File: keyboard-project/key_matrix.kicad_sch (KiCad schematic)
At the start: 0 parts

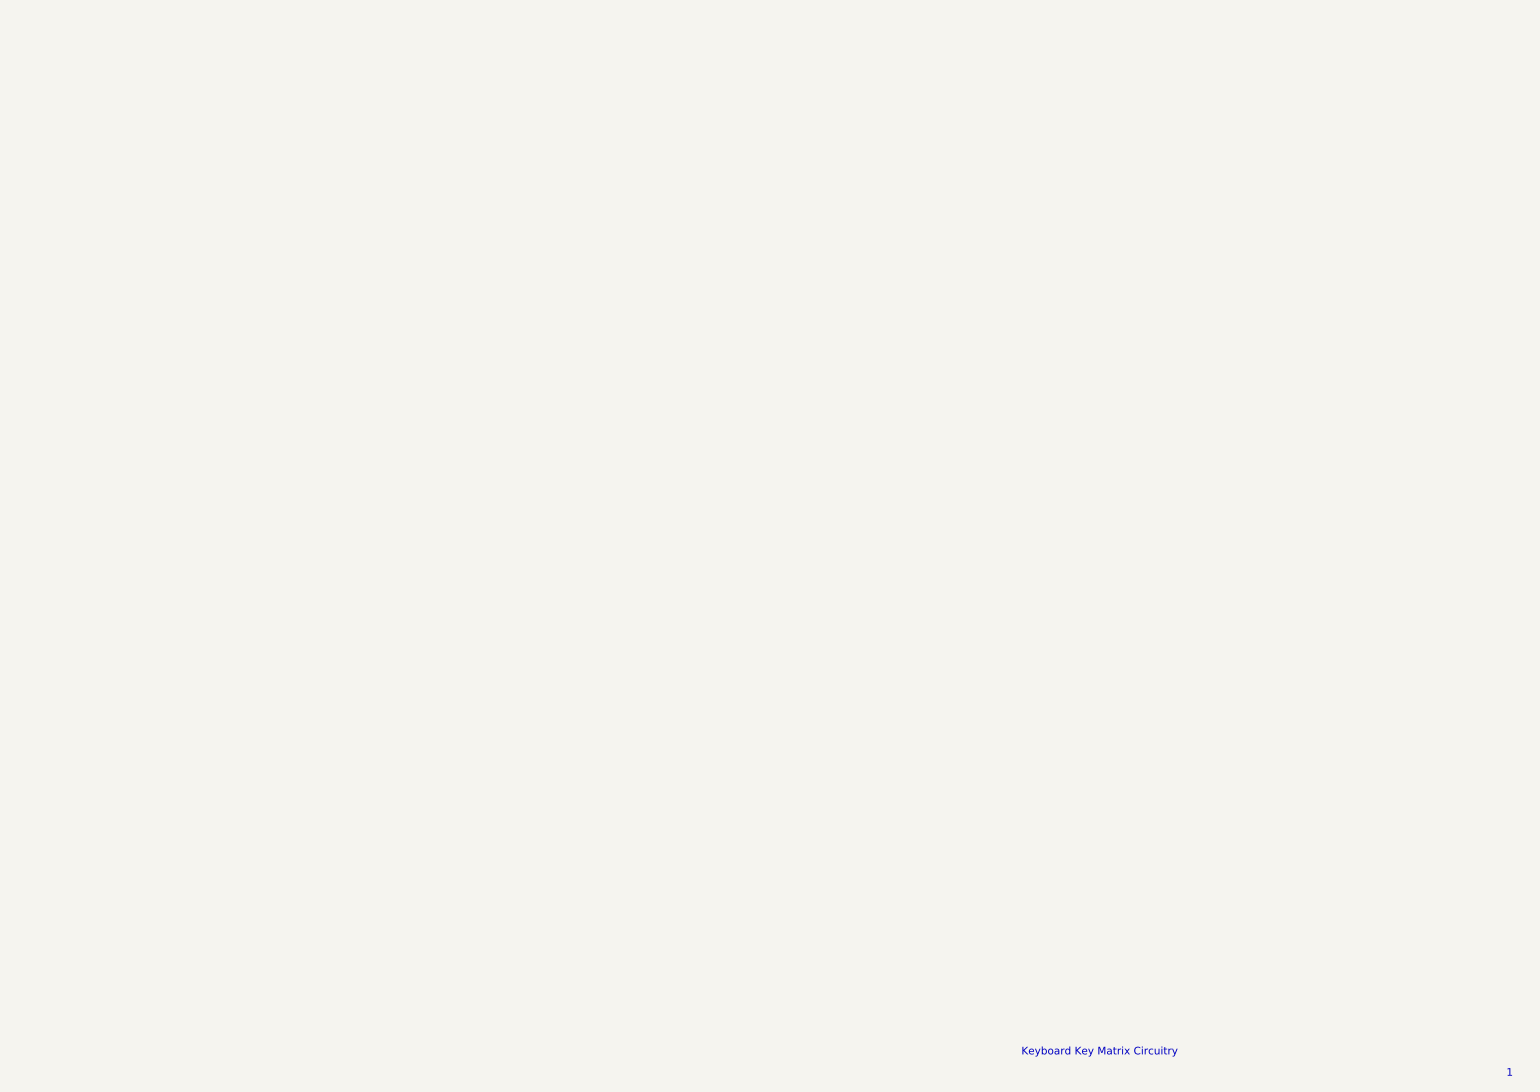
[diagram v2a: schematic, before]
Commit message: encoders, trackball, and display circuits
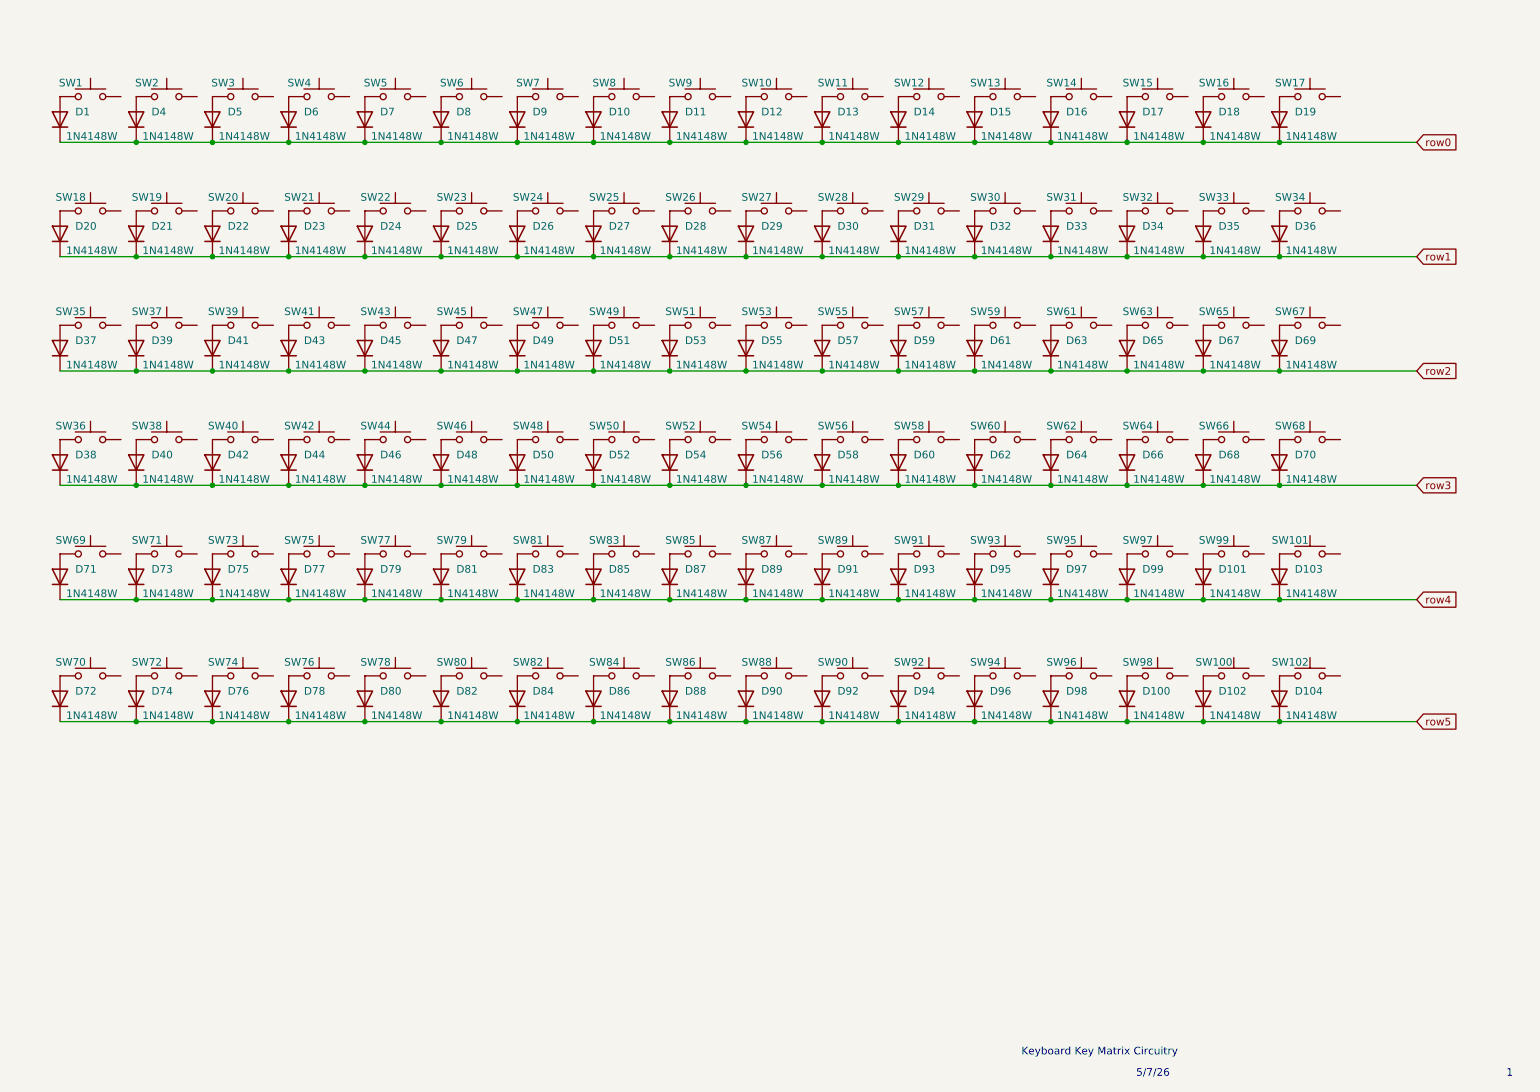
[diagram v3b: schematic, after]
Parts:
- added D1, D10, D100, D101, D102, D103, D104, D11, D12, D13, D14, D15, D16, D17, D18, D19, D20, D21, D22, D23, D24, D25, D26, D27, D28, D29, D30, D31, D32, D33, D34, D35, D36, D37, D38, D39, D4, D40, D41, D42, D43, D44, D45, D46, D47, D48, D49, D5, D50, D51, D52, D53, D54, D55, D56, D57, D58, D59, D6, D60, D61, D62, D63, D64, D65, D66, D67, D68, D69, D7, D70, D71, D72, D73, D74, D75, D76, D77, D78, D79, D8, D80, D81, D82, D83, D84, D85, D86, D87, D88, D89, D9, D90, D91, D92, D93, D94, D95, D96, D97, D98, D99: 1N4148W, Diode_SMD:D_SOD-123, symbol Diode:1N4148W
- added SW1, SW10, SW100, SW101, SW102, SW11, SW12, SW13, SW14, SW15, SW16, SW17, SW18, SW19, SW2, SW20, SW21, SW22, SW23, SW24, SW25, SW26, SW27, SW28, SW29, SW3, SW30, SW31, SW32, SW33, SW34, SW35, SW36, SW37, SW38, SW39, SW4, SW40, SW41, SW42, SW43, SW44, SW45, SW46, SW47, SW48, SW49, SW5, SW50, SW51, SW52, SW53, SW54, SW55, SW56, SW57, SW58, SW59, SW6, SW60, SW61, SW62, SW63, SW64, SW65, SW66, SW67, SW68, SW69, SW7, SW70, SW71, SW72, SW73, SW74, SW75, SW76, SW77, SW78, SW79, SW8, SW80, SW81, SW82, SW83, SW84, SW85, SW86, SW87, SW88, SW89, SW9, SW90, SW91, SW92, SW93, SW94, SW95, SW96, SW97, SW98, SW99: SW_Push, symbol Switch:SW_Push
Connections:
- new net: D39.2 (A), SW37.1
- new net: D42.2 (A), SW40.1
- new net: D32.2 (A), SW30.1
- new net: D50.2 (A), SW48.1
- new net: D51.2 (A), SW49.1
- new net: D41.2 (A), SW39.1
- new net: D26.2 (A), SW24.1
- new net: D27.2 (A), SW25.1
- new net: D1.2 (A), SW1.1
- new net: D7.2 (A), SW5.1
- new net: D28.2 (A), SW26.1
- new net: D18.2 (A), SW16.1
- new net: D38.2 (A), SW36.1
- new net: D98.2 (A), SW96.1
- new net: D104.2 (A), SW102.1
- new net: D24.2 (A), SW22.1
- new net: D36.2 (A), SW34.1
- new net: D17.2 (A), SW15.1
- new net: D19.2 (A), SW17.1
- new net: D53.2 (A), SW51.1
- new net: D40.2 (A), SW38.1
- new net: D82.2 (A), SW80.1
- new net: D55.2 (A), SW53.1
- new net: D64.2 (A), SW62.1
- new net: D57.2 (A), SW55.1
- new net: D61.2 (A), SW59.1
- new net: D20.2 (A), SW18.1
- new net: D102.2 (A), SW100.1
- new net: D31.2 (A), SW29.1
- new net: D94.2 (A), SW92.1
- new net: D21.2 (A), SW19.1
- new net: D78.2 (A), SW76.1
- new net: D48.2 (A), SW46.1
- new net: D62.2 (A), SW60.1
- new net: D97.2 (A), SW95.1
- new net: D88.2 (A), SW86.1
- new net: D45.2 (A), SW43.1
- new net: D5.2 (A), SW3.1
- new net: D11.2 (A), SW9.1
- new net: D95.2 (A), SW93.1
- new net: D29.2 (A), SW27.1
- new net: D63.2 (A), SW61.1
- new net: D75.2 (A), SW73.1
- new net: D84.2 (A), SW82.1
- new net: D86.2 (A), SW84.1
- new net: D70.2 (A), SW68.1
- new net: D92.2 (A), SW90.1
- new net: D83.2 (A), SW81.1
- new net: D80.2 (A), SW78.1
- new net: D44.2 (A), SW42.1
- new net: D16.2 (A), SW14.1
- new net: D14.2 (A), SW12.1
- new net: D81.2 (A), SW79.1
- new net: D66.2 (A), SW64.1
- new net: D96.2 (A), SW94.1
- new net: D67.2 (A), SW65.1
- new net: D68.2 (A), SW66.1
- new net: D9.2 (A), SW7.1
- new net: D49.2 (A), SW47.1
- new net: D6.2 (A), SW4.1
- new net: D12.2 (A), SW10.1
- new net: D54.2 (A), SW52.1
- new net: D59.2 (A), SW57.1
- new net: D65.2 (A), SW63.1
- new net: D47.2 (A), SW45.1
- new net: D58.2 (A), SW56.1
- new net: D101.2 (A), SW99.1
- new net: D8.2 (A), SW6.1
- new net: D103.2 (A), SW101.1
- new net: D74.2 (A), SW72.1
- new net: D37.2 (A), SW35.1
- new net: D91.2 (A), SW89.1
- new net: D72.2 (A), SW70.1
- new net: D71.2 (A), SW69.1
- new net: D77.2 (A), SW75.1
- new net: D73.2 (A), SW71.1
- new net: D87.2 (A), SW85.1
- new net: D100.2 (A), SW98.1
- new net: D25.2 (A), SW23.1
- new net: D85.2 (A), SW83.1
- new net: D4.2 (A), SW2.1
- new net: D15.2 (A), SW13.1
- new net: D43.2 (A), SW41.1
- new net: D34.2 (A), SW32.1
- new net: D69.2 (A), SW67.1
- new net: D60.2 (A), SW58.1
- new net: D79.2 (A), SW77.1
- new net: D89.2 (A), SW87.1
- new net: D10.2 (A), SW8.1
- new net: D30.2 (A), SW28.1
- new net: D56.2 (A), SW54.1
- new net: D46.2 (A), SW44.1
- new net: D13.2 (A), SW11.1
- new net: D99.2 (A), SW97.1
- new net: D90.2 (A), SW88.1
- new net: D22.2 (A), SW20.1
- new net: D35.2 (A), SW33.1
- new net: D52.2 (A), SW50.1
- new net: D93.2 (A), SW91.1
- new net: D23.2 (A), SW21.1
- new net: D76.2 (A), SW74.1
- new net: D33.2 (A), SW31.1
- new net row0: D1.1 (K), D10.1 (K), D11.1 (K), D12.1 (K), D13.1 (K), D14.1 (K), D15.1 (K), D16.1 (K), D17.1 (K), D18.1 (K), D19.1 (K), D4.1 (K), D5.1 (K), D6.1 (K), D7.1 (K), D8.1 (K), D9.1 (K)
- new net row1: D20.1 (K), D21.1 (K), D22.1 (K), D23.1 (K), D24.1 (K), D25.1 (K), D26.1 (K), D27.1 (K), D28.1 (K), D29.1 (K), D30.1 (K), D31.1 (K), D32.1 (K), D33.1 (K), D34.1 (K), D35.1 (K), D36.1 (K)
- new net row2: D37.1 (K), D39.1 (K), D41.1 (K), D43.1 (K), D45.1 (K), D47.1 (K), D49.1 (K), D51.1 (K), D53.1 (K), D55.1 (K), D57.1 (K), D59.1 (K), D61.1 (K), D63.1 (K), D65.1 (K), D67.1 (K), D69.1 (K)
- new net row3: D38.1 (K), D40.1 (K), D42.1 (K), D44.1 (K), D46.1 (K), D48.1 (K), D50.1 (K), D52.1 (K), D54.1 (K), D56.1 (K), D58.1 (K), D60.1 (K), D62.1 (K), D64.1 (K), D66.1 (K), D68.1 (K), D70.1 (K)
- new net row4: D101.1 (K), D103.1 (K), D71.1 (K), D73.1 (K), D75.1 (K), D77.1 (K), D79.1 (K), D81.1 (K), D83.1 (K), D85.1 (K), D87.1 (K), D89.1 (K), D91.1 (K), D93.1 (K), D95.1 (K), D97.1 (K), D99.1 (K)
- new net row5: D100.1 (K), D102.1 (K), D104.1 (K), D72.1 (K), D74.1 (K), D76.1 (K), D78.1 (K), D80.1 (K), D82.1 (K), D84.1 (K), D86.1 (K), D88.1 (K), D90.1 (K), D92.1 (K), D94.1 (K), D96.1 (K), D98.1 (K)
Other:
- note added: "5/7/26"

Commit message: all footprints in now
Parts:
- removed D101, D102, D103, D104, D16, D64, D66, D68, D70, D78, D80, D84, D86: 1N4148W, Diode_SMD:D_SOD-123, symbol Diode:1N4148W
- removed SW100, SW101, SW102, SW90, SW91, SW92, SW93, SW94, SW95, SW96, SW97, SW98, SW99: SW_Push, symbol Switch:SW_Push
- SW1, SW10, SW11, SW12, SW13, SW14, SW15, SW16, SW17, SW18, SW19, SW2, SW20, SW21, SW22, SW23, SW24, SW25, SW26, SW27, SW28, SW29, SW3, SW31, SW32, SW33, SW34, SW35, SW36, SW37, SW38, SW39, SW4, SW40, SW41, SW42, SW43, SW44, SW45, SW46, SW47, SW48, SW5, SW51, SW52, SW53, SW54, SW55, SW56, SW57, SW58, SW59, SW6, SW60, SW61, SW65, SW66, SW67, SW68, SW69, SW7, SW70, SW71, SW72, SW73, SW74, SW76, SW77, SW78, SW79, SW8, SW88, SW89, SW9: footprint (none) -> Button_Switch_Keyboard:SW_Cherry_MX_1.00u_PCB
- SW30: footprint (none) -> Button_Switch_Keyboard:SW_Cherry_MX_2.00u_PCB
- SW49, SW50: footprint (none) -> Button_Switch_Keyboard:SW_Cherry_MX_1.50u_PCB
- SW62, SW64: footprint (none) -> Button_Switch_Keyboard:SW_Cherry_MX_2.25u_PCB
- SW63: footprint (none) -> Button_Switch_Keyboard:SW_Cherry_MX_1.75u_PCB
- SW75: footprint (none) -> Button_Switch_Keyboard:SW_Cherry_MX_2.75u_PCB
- SW80, SW81, SW82, SW83, SW84, SW85, SW86: footprint (none) -> Button_Switch_Keyboard:SW_Cherry_MX_1.25u_PCB
- SW87: footprint (none) -> Button_Switch_Keyboard:SW_Cherry_MX_6.25u_PCB
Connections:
- net at D39.2 (A): now also SW34.1; no longer SW37.1
- net Matrix Col 4: now reaches SW37.2
- net Matrix Col 4: now also SW21.2, SW5.2, SW54.2, SW68.2
- net at D42.2 (A): now also SW52.1; no longer SW40.1
- net at D32.2 (A): now also SW29.1; no longer SW30.1
- net Matrix Col 13: now reaches SW30.2
- net Matrix Col 13: now also SW49.2, SW76.2
- net at D50.2 (A): now also SW56.1; no longer SW48.1
- net at D51.2 (A): now also SW40.1; no longer SW49.1
- net at D41.2 (A): now also SW35.1; no longer SW39.1
- net Matrix Col 6: now reaches SW39.2
- net Matrix Col 6: now also SW23.2, SW56.2, SW7.2, SW70.2
- net at D26.2 (A): now also SW23.1; no longer SW24.1
- net at SW25.1: now also D28.2 (A); no longer D27.2 (A)
- net Matrix Col 8: now reaches SW25.2
- net Matrix Col 8: now also SW41.2, SW58.2, SW72.2, SW83.2, SW9.2
- net at SW26.1: now also D29.2 (A); no longer D28.2 (A)
- net at SW16.1: now also D19.2 (A); no longer D18.2 (A)
- net Matrix Col 16: now reaches SW16.2
- net Matrix Col 16: now also SW33.2, SW48.2, SW79.2
- net at D38.2 (A): now also SW63.1; no longer SW36.1
- net at D98.2 (A): now also SW77.1
- net at D24.2 (A): now also SW21.1; no longer SW22.1
- net at D36.2 (A): now also SW33.1; no longer SW34.1
- net Matrix Col 1: now reaches SW34.2
- net Matrix Col 1: now also SW18.2, SW2.2, SW51.2, SW65.2, SW81.2
- net at D17.2 (A): now also SW14.1; no longer SW15.1
- net at SW17.1: now also D20.2 (A); no longer D19.2 (A)
- net at D53.2 (A): now also SW41.1; no longer SW51.1
- net at SW38.1: now also D47.2 (A); no longer D40.2 (A)
- net Matrix Col 5: now reaches SW38.2
- net Matrix Col 5: now also SW22.2, SW55.2, SW6.2, SW69.2, SW87.2
- net at SW80.1: now also D72.2 (A); no longer D82.2 (A)
- net at D55.2 (A): now also SW42.1; no longer SW53.1
- net Matrix Col 3: now reaches SW53.2
- net Matrix Col 3: now also SW20.2, SW36.2, SW4.2, SW67.2
- net at SW62.1: now also D62.2 (A)
- net Matrix Col 12: now reaches SW62.2
- net Matrix Col 12: now also SW13.2, SW29.2, SW45.2
- net at SW55.1: now also D48.2 (A); no longer D57.2 (A)
- net at D61.2 (A): now also SW45.1; no longer SW59.1
- net Matrix Col 9: now reaches SW59.2
- net Matrix Col 9: now also SW10.2, SW26.2, SW42.2, SW73.2, SW84.2
- net at SW18.1: now also D21.2 (A); no longer D20.2 (A)
- net at D31.2 (A): now also SW28.1; no longer SW29.1
- net at D94.2 (A): now also SW86.1
- net at SW19.1: now also D22.2 (A); no longer D21.2 (A)
- net Matrix Col 2: now reaches SW19.2
- net Matrix Col 2: now also SW3.2, SW35.2, SW52.2, SW66.2, SW82.2
- net at SW76.1: now also D95.2 (A)
- net at SW46.1: now also D65.2 (A); no longer D48.2 (A)
- net Matrix Col 14: now reaches SW46.2
- net Matrix Col 14: now also SW14.2, SW31.2, SW77.2
- net at SW60.1: now also D58.2 (A); no longer D62.2 (A)
- net Matrix Col 10: now reaches SW60.2
- net Matrix Col 10: now also SW11.2, SW27.2, SW43.2, SW74.2, SW85.2
- net at D97.2 (A): now also SW89.1
- net at D88.2 (A): now also SW83.1; no longer SW86.1
- net Matrix Col 11: now reaches SW86.2
- net Matrix Col 11: now also SW12.2, SW28.2, SW44.2, SW61.2, SW75.2
- net at D45.2 (A): now also SW37.1; no longer SW43.1
- net at SW27.1: now also D30.2 (A); no longer D29.2 (A)
- net at SW61.1: now also D60.2 (A); no longer D63.2 (A)
- net at SW73.1: now also D89.2 (A); no longer D75.2 (A)
- net at SW82.1: now also D76.2 (A)
- net Matrix Col 7: now reaches SW24.2
- net Matrix Col 7: now also SW40.2, SW57.2, SW71.2, SW8.2
- net at SW84.1: now also D90.2 (A)
- net at SW68.1: now also D79.2 (A)
- net at D92.2 (A): now also SW85.1
- net at SW81.1: now also D74.2 (A); no longer D83.2 (A)
- net at SW78.1: now also D99.2 (A)
- net at D44.2 (A): now also SW53.1; no longer SW42.1
- net at SW79.1: now also D100.2 (A); no longer D81.2 (A)
- net at SW64.1: now also D71.2 (A)
- net at D96.2 (A): now also SW88.1
- net at D67.2 (A): now also SW47.1; no longer SW65.1
- net at SW66.1: now also D75.2 (A)
- net at D49.2 (A): now also SW39.1; no longer SW47.1
- net Matrix Col 15: now reaches SW47.2
- net Matrix Col 15: now also SW15.2, SW32.2, SW78.2
- net at D54.2 (A): now also SW58.1; no longer SW52.1
- net at D59.2 (A): now also SW44.1; no longer SW57.1
- net at SW72.1: now also D87.2 (A); no longer D74.2 (A)
- net at D37.2 (A): now also SW50.1; no longer SW35.1
- net at D91.2 (A): now also SW74.1; no longer SW89.1
- net at SW70.1: now also D83.2 (A); no longer D72.2 (A)
- net at SW69.1: now also D81.2 (A); no longer D71.2 (A)
- net at D77.2 (A): now also SW67.1; no longer SW75.1
- net at D73.2 (A): now also SW65.1; no longer SW71.1
- net at D25.2 (A): now also SW22.1; no longer SW23.1
- net at D85.2 (A): now also SW71.1; no longer SW83.1
- net at D43.2 (A): now also SW36.1; no longer SW41.1
- net at D34.2 (A): now also SW31.1; no longer SW32.1
- net Matrix Col 0: now reaches SW17.2
- net Matrix Col 0: now also SW1.2, SW50.2, SW63.2, SW64.2, SW80.2
- net at D69.2 (A): now also SW48.1; no longer SW67.1
- net at SW87.1: now also D82.2 (A); no longer D89.2 (A)
- net at D56.2 (A): now also SW59.1; no longer SW54.1
- net at D46.2 (A): now also SW54.1; no longer SW44.1
- net at SW20.1: now also D23.2 (A); no longer D22.2 (A)
- net at D35.2 (A): now also SW32.1; no longer SW33.1
- net at D52.2 (A): now also SW57.1; no longer SW50.1
- net at D93.2 (A): now also SW75.1
- net at D33.2 (A): now also SW30.1; no longer SW31.1
- net row0 renamed Matrix Row 0
- net row1 renamed Matrix Row 1
- net row2 renamed Matrix Row 2
- net row3 renamed Matrix Row 3
- net row4 renamed Matrix Row 4
- net Matrix Row 4: no longer D97.1 (K), D99.1 (K)
- net row5 renamed Matrix Row 5
- net Matrix Row 5: now also D97.1 (K), D99.1 (K)
- new net: D27.2 (A), SW24.1
- new net: D18.2 (A), SW15.1
- new net: D63.2 (A), SW49.1
- new net: D57.2 (A), SW43.1
- new net: D40.2 (A), SW51.1
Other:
- note added: "'""
- note added: ",<"
- note added: "-_"
- note added: ".>"
- note added: "/?"
- note added: "0"
- note added: "2"
- note added: "3"
- note added: "4"
- note added: "5"
- note added: "6"
- note added: "7"
- note added: "8"
- note added: "9"
- note added: ";:"
- note added: "=+"
- note added: "A"
- note added: "B"
- note added: "Backspace"
- note added: "C"
- note added: "Caps Lck"
- note added: "Context"
- note added: "D"
- note added: "Del"
- note added: "Down Arrow"
- note added: "E"
- note added: "ESC"
- note added: "End"
- note added: "Enter"
- note added: "F"
- note added: "F1"
- note added: "F10"
- note added: "F11"
- note added: "F12"
- note added: "F2"
- note added: "F3"
- note added: "F4"
- note added: "F5"
- note added: "F6"
- note added: "F7"
- note added: "F8"
- note added: "F9"
- note added: "G"
- note added: "H"
- note added: "Home"
- note added: "I"
- note added: "Ins"
- note added: "J"
- note added: "K"
- note added: "L"
- note added: "L Alt"
- note added: "L Ctrl"
- note added: "L Shift"
- note added: "L Win"
- note added: "L-Click"
- note added: "Left Arrow"
- note added: "M"
- note added: "N"
- note added: "O"
- note added: "P"
- note added: "Page Down"
- note added: "Page Up"
- note added: "Pause/Break"
- note added: "Print Screen"
- note added: "Q"
- note added: "R"
- note added: "R Alt"
- note added: "R Ctrl"
- note added: "R Shift"
- note added: "R Win"
- note added: "R-Click"
- note added: "Right Arrow"
- note added: "S"
- note added: "Scroll Lck"
- note added: "Space"
- note added: "T"
- note added: "Tab"
- note added: "U"
- note added: "Up Arrow"
- note added: "V"
- note added: "W"
- note added: "X"
- note added: "Y"
- note added: "Z"
- note added: "[{"
- note added: "\|"
- note added: "]}"
- note added: "`~"
- moved on the sheet: D95
